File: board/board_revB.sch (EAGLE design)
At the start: 79 parts, among them Q1 ULN2003AS, Q2 ULN2003AD, Y1 8Mhz

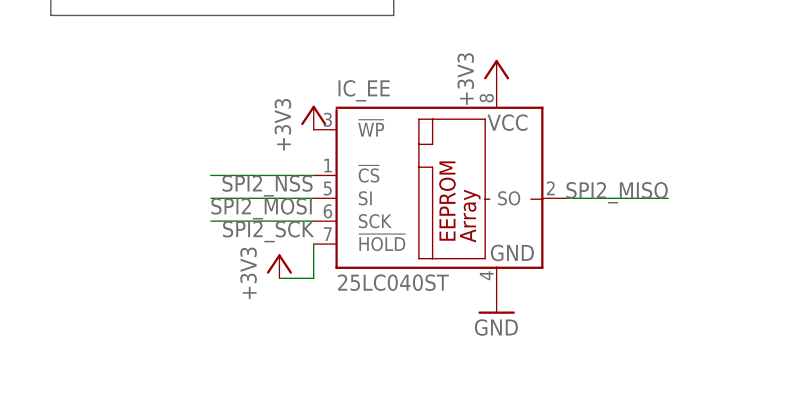
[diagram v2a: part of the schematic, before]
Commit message: [GUI] Working on XML file saving
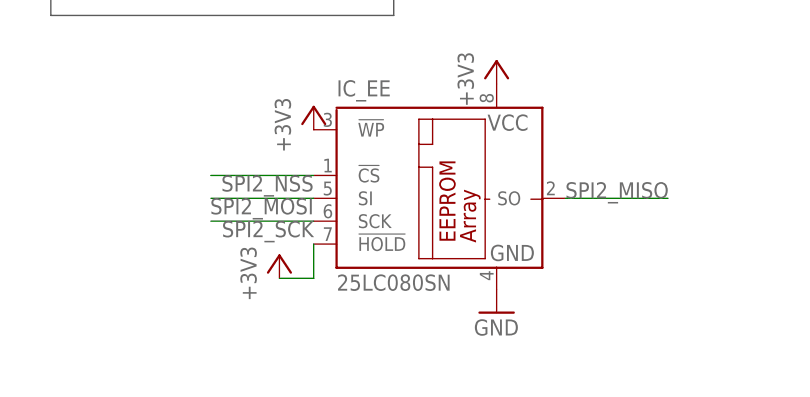
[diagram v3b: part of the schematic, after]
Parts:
- IC_EE: value 25LC040ST -> 25LC080SN; device microchip:25LC040ST -> microchip:25LC080SN
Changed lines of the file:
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@@
 <?xml version="1.0" encoding="utf-8"?>
 <!DOCTYPE eagle SYSTEM "eagle.dtd">
-<eagle version="7.0.0">
+<eagle version="7.1.0">
 <drawing>
 <settings>
@@
 <grid distance="0.05" unitdist="inch" unit="inch" style="lines" multiple="1" display="yes" altdistance="0.005" altunitdist="inch" altunit="inch"/>
 <layers>
-<layer number="1" name="Top" color="4" fill="1" visible="no" active="no"/>
-<layer number="2" name="Route2" color="1" fill="3" visible="no" active="no"/>
-<layer number="3" name="Route3" color="4" fill="3" visible="no" active="no"/>
-<layer number="4" name="Route4" color="1" fill="4" visible="no" active="no"/>
-<layer number="5" name="Route5" color="4" fill="4" visible="no" active="no"/>
-<layer number="6" name="Route6" color="1" fill="8" visible="no" active="no"/>
-<layer number="7" name="Route7" color="4" fill="8" visible="no" active="no"/>
-<layer number="8" name="Route8" color="1" fill="2" visible="no" active="no"/>
-<layer number="9" name="Route9" color="4" fill="2" visible="no" active="no"/>
-<layer number="10" name="Route10" color="1" fill="7" visible="no" active="no"/>
-<layer number="11" name="Route11" color="4" fill="7" visible="no" active="no"/>
-<layer number="12" name="Route12" color="1" fill="5" visible="no" active="no"/>
-<layer number="13" name="Route13" color="4" fill="5" visible="no" active="no"/>
-<layer number="14" name="Route14" color="1" fill="6" visible="no" active="no"/>
-<layer number="15" name="Route15" color="4" fill="6" visible="no" active="no"/>
-<layer number="16" name="Bottom" color="1" fill="1" visible="no" active="no"/>
-<layer number="17" name="Pads" color="2" fill="1" visible="no" active="no"/>
-<layer number="18" name="Vias" color="2" fill="1" visible="no" active="no"/>
-<layer number="19" name="Unrouted" color="6" fill="1" visible="no" active="no"/>
-<layer number="20" name="Dimension" color="15" fill="1" visible="no" active="no"/>
-<layer number="21" name="tPlace" color="16" fill="1" visible="no" active="no"/>
-<layer number="22" name="bPlace" color="14" fill="1" visible="no" active="no"/>
-<layer number="23" name="tOrigins" color="15" fill="1" visible="no" active="no"/>
-<layer number="24" name="bOrigins" color="15" fill="1" visible="no" active="no"/>
-<layer number="25" name="tNames" color="7" fill="1" visible="no" active="no"/>
-<layer number="26" name="bNames" color="7" fill="1" visible="no" active="no"/>
-<layer number="27" name="tValues" color="7" fill="1" visible="no" active="no"/>
-<layer number="28" name="bValues" color="7" fill="1" visible="no" active="no"/>
+<layer number="1" name="Top" color="4" fill="1" visible="yes" active="no"/>
+<layer number="2" name="Route2" color="1" fill="3" visible="yes" active="no"/>
+<layer number="3" name="Route3" color="4" fill="3" visible="yes" active="no"/>
+<layer number="4" name="Route4" color="1" fill="4" visible="yes" active="no"/>
+<layer number="5" name="Route5" color="4" fill="4" visible="yes" active="no"/>
+<layer number="6" name="Route6" color="1" fill="8" visible="yes" active="no"/>
+<layer number="7" name="Route7" color="4" fill="8" visible="yes" active="no"/>
+<layer number="8" name="Route8" color="1" fill="2" visible="yes" active="no"/>
+<layer number="9" name="Route9" color="4" fill="2" visible="yes" active="no"/>
+<layer number="10" name="Route10" color="1" fill="7" visible="yes" active="no"/>
+<layer number="11" name="Route11" color="4" fill="7" visible="yes" active="no"/>
+<layer number="12" name="Route12" color="1" fill="5" visible="yes" active="no"/>
+<layer number="13" name="Route13" color="4" fill="5" visible="yes" active="no"/>
+<layer number="14" name="Route14" color="1" fill="6" visible="yes" active="no"/>
+<layer number="15" name="Route15" color="4" fill="6" visible="yes" active="no"/>
+<layer number="16" name="Bottom" color="1" fill="1" visible="yes" active="no"/>
+<layer number="17" name="Pads" color="2" fill="1" visible="yes" active="no"/>
+<layer number="18" name="Vias" color="2" fill="1" visible="yes" active="no"/>
+<layer number="19" name="Unrouted" color="6" fill="1" visible="yes" active="no"/>
+<layer number="20" name="Dimension" color="15" fill="1" visible="yes" active="no"/>
+<layer number="21" name="tPlace" color="16" fill="1" visible="yes" active="no"/>
+<layer number="22" name="bPlace" color="14" fill="1" visible="yes" active="no"/>
+<layer number="23" name="tOrigins" color="15" fill="1" visible="yes" active="no"/>
+<layer number="24" name="bOrigins" color="15" fill="1" visible="yes" active="no"/>
+<layer number="25" name="tNames" color="7" fill="1" visible="yes" active="no"/>
+<layer number="26" name="bNames" color="7" fill="1" visible="yes" active="no"/>
+<layer number="27" name="tValues" color="7" fill="1" visible="yes" active="no"/>
+<layer number="28" name="bValues" color="7" fill="1" visible="yes" active="no"/>
 <layer number="29" name="tStop" color="7" fill="3" visible="no" active="no"/>
 <layer number="30" name="bStop" color="7" fill="6" visible="no" active="no"/>
@@
 <layer number="35" name="tGlue" color="7" fill="4" visible="no" active="no"/>
 <layer number="36" name="bGlue" color="7" fill="5" visible="no" active="no"/>
-<layer number="37" name="tTest" color="7" fill="1" visible="no" active="no"/>
-<layer number="38" name="bTest" color="7" fill="1" visible="no" active="no"/>
+<layer number="37" name="tTest" color="7" fill="1" visible="yes" active="no"/>
+<layer number="38" name="bTest" color="7" fill="1" visible="yes" active="no"/>
 <layer number="39" name="tKeepout" color="4" fill="11" visible="no" active="no"/>
 <layer number="40" name="bKeepout" color="1" fill="11" visible="no" active="no"/>
@@
 <layer number="44" name="Drills" color="7" fill="1" visible="no" active="no"/>
 <layer number="45" name="Holes" color="7" fill="1" visible="no" active="no"/>
-<layer number="46" name="Milling" color="3" fill="1" visible="no" active="no"/>
-<layer number="47" name="Measures" color="7" fill="1" visible="no" active="no"/>
-<layer number="48" name="Document" color="7" fill="1" visible="no" active="no"/>
-<layer number="49" name="Reference" color="7" fill="1" visible="no" active="no"/>
-<layer number="50" name="dxf" color="7" fill="1" visible="no" active="no"/>
-<layer number="51" name="tDocu" color="6" fill="1" visible="no" active="no"/>
-<layer number="52" name="bDocu" color="7" fill="1" visible="no" active="no"/>
-<layer number="53" name="tGND_GNDA" color="7" fill="9" visible="no" active="no"/>
-<layer number="54" name="bGND_GNDA" color="1" fill="9" visible="no" active="no"/>
-<layer number="56" name="wert" color="7" fill="1" visible="no" active="no"/>
-<layer number="57" name="tCAD" color="7" fill="1" visible="no" active="no"/>
+<layer number="46" name="Milling" color="3" fill="1" visible="yes" active="no"/>
+<layer number="47" name="Measures" color="7" fill="1" visible="yes" active="no"/>
+<layer number="48" name="Document" color="7" fill="1" visible="yes" active="no"/>
+<layer number="49" name="Reference" color="7" fill="1" visible="yes" active="no"/>
+<layer number="50" name="dxf" color="7" fill="1" visible="yes" active="no"/>
+<layer number="51" name="tDocu" color="6" fill="1" visible="yes" active="no"/>
+<layer number="52" name="bDocu" color="7" fill="1" visible="yes" active="no"/>
+<layer number="53" name="tGND_GNDA" color="7" fill="9" visible="yes" active="no"/>
+<layer number="54" name="bGND_GNDA" color="1" fill="9" visible="yes" active="no"/>
+<layer number="56" name="wert" color="7" fill="1" visible="yes" active="no"/>
+<layer number="57" name="tCAD" color="7" fill="1" visible="yes" active="no"/>
 <layer number="91" name="Nets" color="2" fill="1" visible="yes" active="yes"/>
 <layer number="92" name="Busses" color="1" fill="1" visible="yes" active="yes"/>
@@
 <part name="+3V6" library="supply1" deviceset="+3V3" device=""/>
 <part name="GND22" library="supply1" deviceset="GND" device=""/>
-<part name="IC_EE" library="microchip" deviceset="25*" device="ST" technology="LC040"/>
 <part name="+3V16" library="supply1" deviceset="+3V3" device=""/>
 <part name="+3V18" library="supply1" deviceset="+3V3" device=""/>
+<part name="IC_EE" library="microchip" deviceset="25*" device="SN" technology="LC080"/>
 </parts>
 <sheets>
@@
 <instance part="+3V6" gate="G$1" x="264.16" y="38.1"/>
 <instance part="GND22" gate="1" x="264.16" y="10.16"/>
-<instance part="IC_EE" gate="G$1" x="256.54" y="22.86"/>
 <instance part="+3V16" gate="G$1" x="243.84" y="33.02"/>
 <instance part="+3V18" gate="G$1" x="240.03" y="16.51"/>
+<instance part="IC_EE" gate="G$1" x="256.54" y="22.86"/>
 </instances>
 <busses>
@@
 </segment>
 <segment>
+<pinref part="GND22" gate="1" pin="GND"/>
 <pinref part="IC_EE" gate="G$1" pin="GND"/>
-<pinref part="GND22" gate="1" pin="GND"/>
 </segment>
 </net>
@@
 </segment>
 <segment>
+<pinref part="+3V18" gate="G$1" pin="+3V3"/>
+<wire x1="240.03" y1="13.97" x2="243.84" y2="13.97" width="0.1524" layer="91"/>
+<wire x1="243.84" y1="13.97" x2="243.84" y2="17.78" width="0.1524" layer="91"/>
+<pinref part="IC_EE" gate="G$1" pin="!HOLD"/>
+</segment>
+<segment>
 <pinref part="+3V6" gate="G$1" pin="+3V3"/>
 <pinref part="IC_EE" gate="G$1" pin="VCC"/>
 </segment>
 <segment>
+<pinref part="+3V16" gate="G$1" pin="+3V3"/>
 <pinref part="IC_EE" gate="G$1" pin="!WP"/>
-<pinref part="+3V16" gate="G$1" pin="+3V3"/>
-</segment>
-<segment>
-<pinref part="+3V18" gate="G$1" pin="+3V3"/>
-<pinref part="IC_EE" gate="G$1" pin="!HOLD"/>
-<wire x1="240.03" y1="13.97" x2="243.84" y2="13.97" width="0.1524" layer="91"/>
-<wire x1="243.84" y1="13.97" x2="243.84" y2="17.78" width="0.1524" layer="91"/>
 </segment>
 </net>
@@
 <segment>
 <label x="243.84" y="25.4" size="1.778" layer="95" rot="R180"/>
+<wire x1="232.41" y1="25.4" x2="243.84" y2="25.4" width="0.1524" layer="91"/>
 <pinref part="IC_EE" gate="G$1" pin="!CS"/>
-<wire x1="232.41" y1="25.4" x2="243.84" y2="25.4" width="0.1524" layer="91"/>
-</segment>
-</net>
+</segment>
+</net>

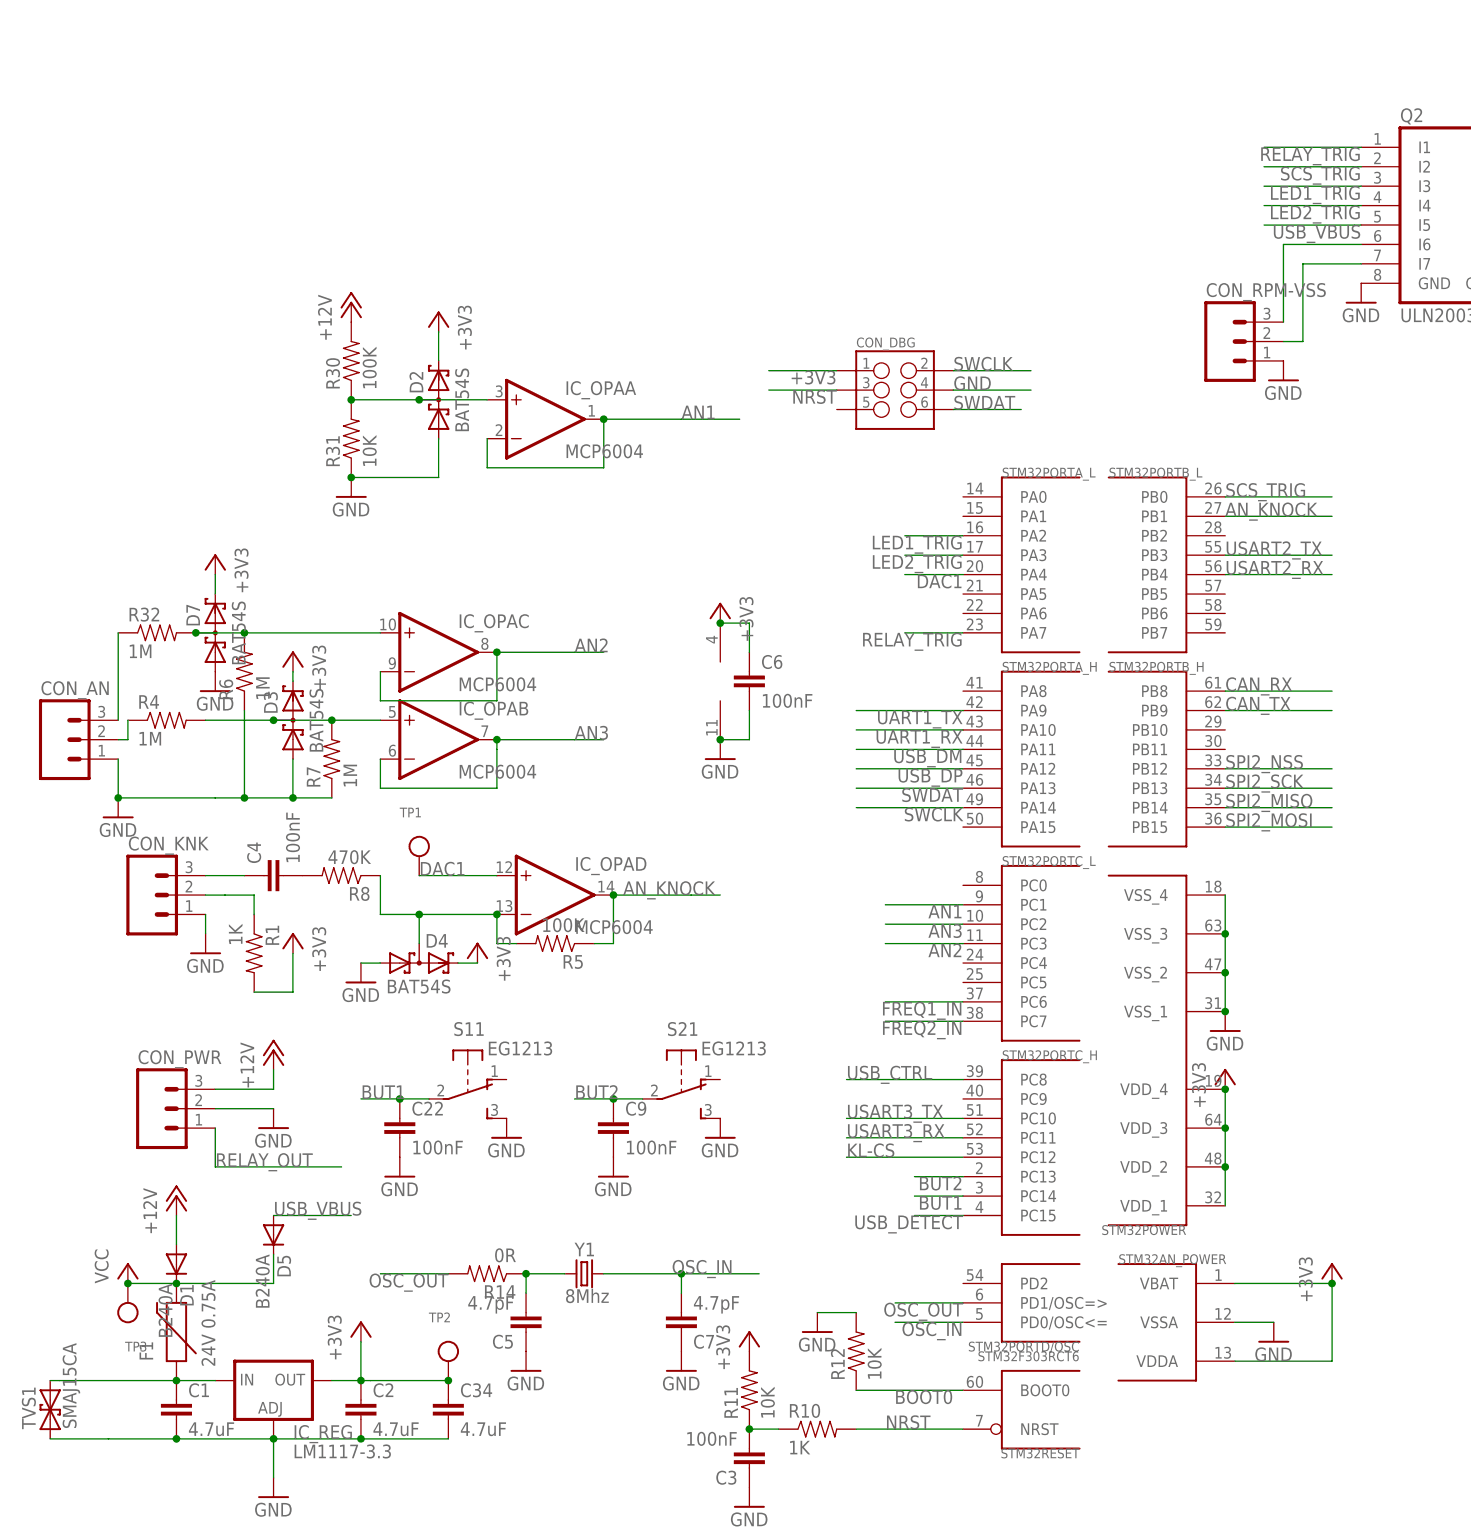
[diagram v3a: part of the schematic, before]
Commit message: [GUI/Code] Rewrote DSP functions, switched to float; Updated DSP library
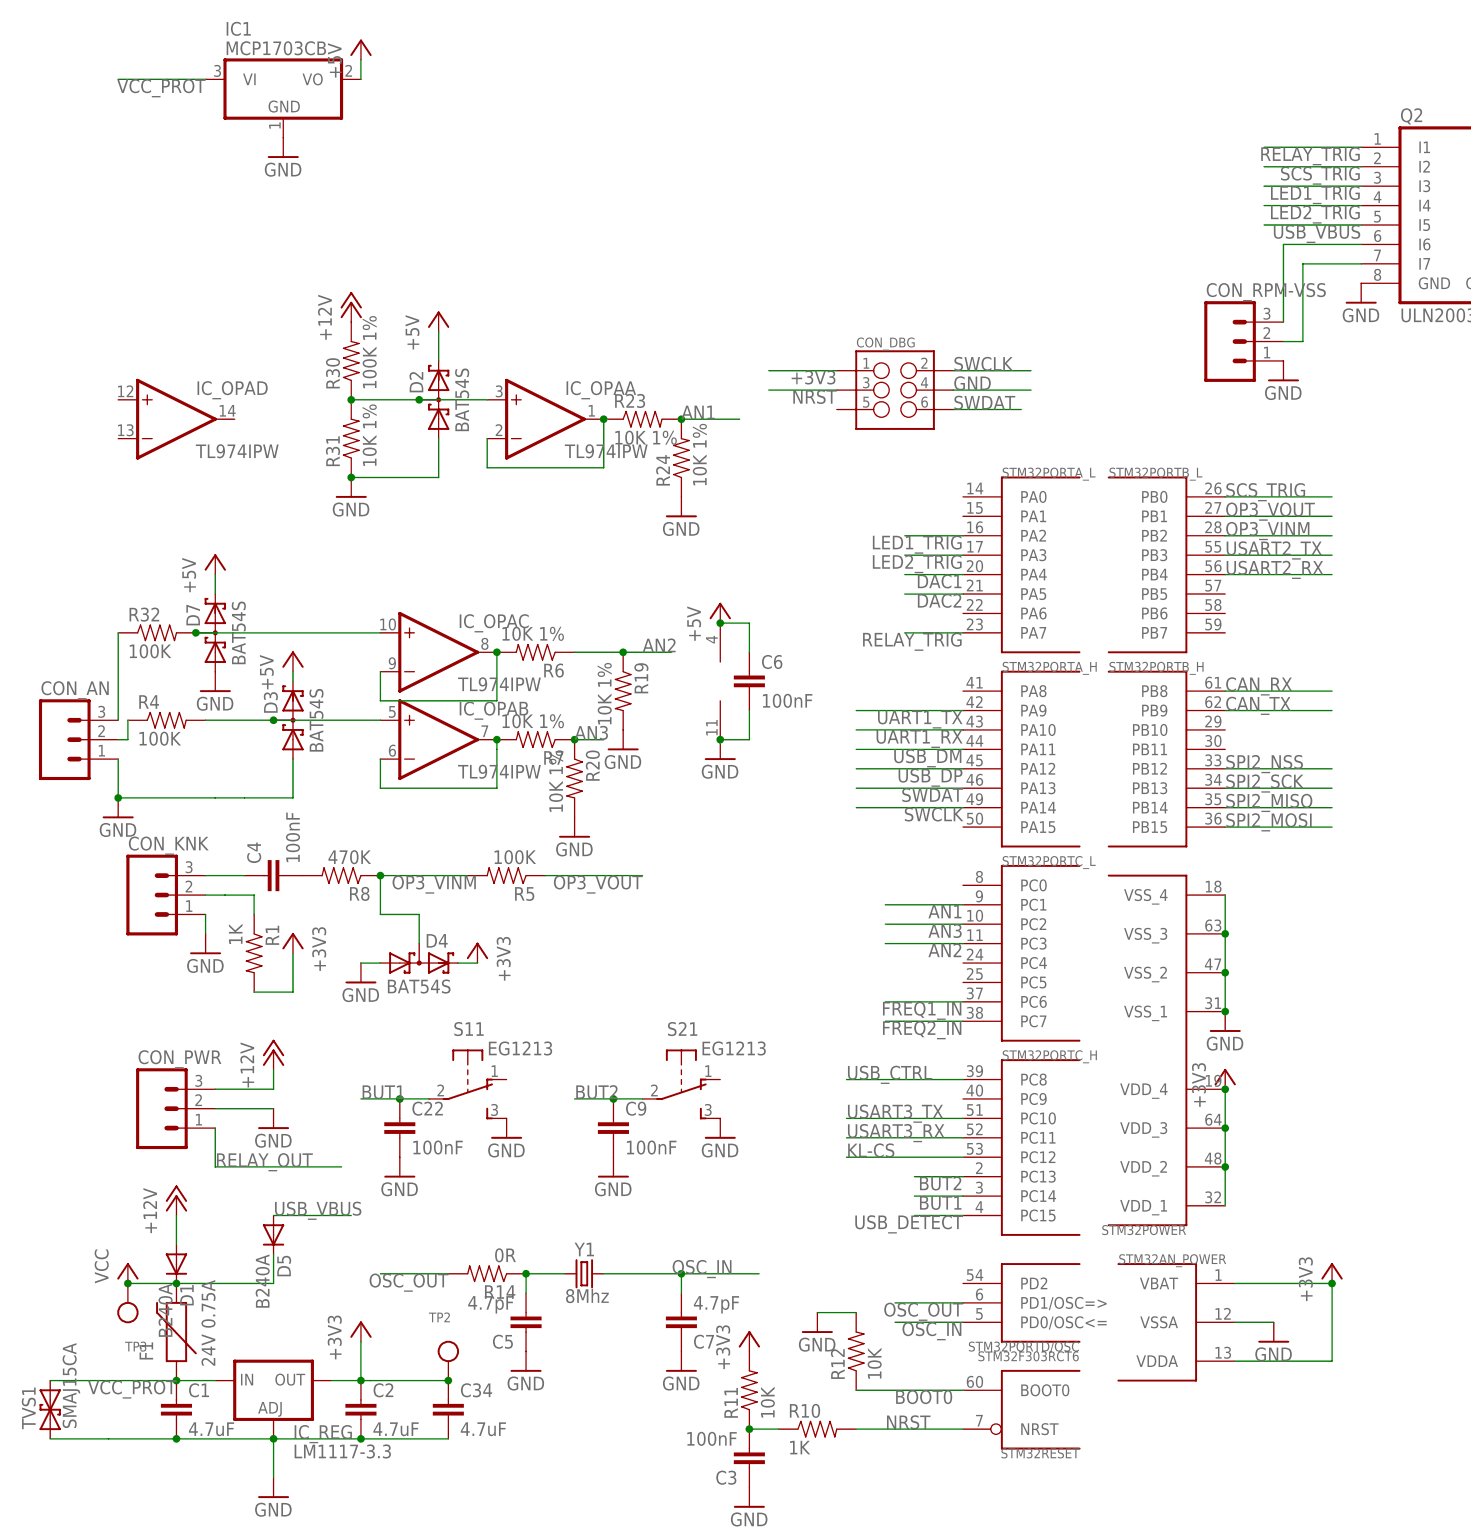
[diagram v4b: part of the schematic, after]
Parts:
- removed TP1: (no value), microbuilder:TESTPOINTROUND1MM
- added IC1: MCP1703CB, linear:MCP1703CB
- added R19, R20, R23, R24: 10K 1%, SparkFun-Resistors:RESISTOR0603-RES
- IC_OPA: value MCP6004 -> TL974IPW
- R30: value 100K -> 100K 1%
- R31: value 10K -> 10K 1%
- R32, R4: value 1M -> 100K
- R6, R7: value 1M -> 10K 1%
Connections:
- removed net AN_KNOCK: IC_OPAD.OUT, R5.1, STM32PORTB_L.PB1
- removed net N$12: D4.C1A2, IC_OPAD.-IN, R5.2, R8.1
- removed net N$20: C1.1, F1.1, IC_REG.IN, TVS1.2
- new net +5V: C6.1, D2.C2, D3.C2, D7.C2, IC1.VO, IC_OPAP.V+
- new net AN1_N: IC_OPAA.-IN, IC_OPAA.OUT, R23.1
- new net AN2_N: IC_OPAC.-IN, IC_OPAC.OUT, R6.2
- new net AN3_N: IC_OPAB.-IN, IC_OPAB.OUT, R7.2
- new net DAC2: STM32PORTA_L.PA5
- new net OP3_VINM: D4.C1A2, R5.2, R8.1, STM32PORTB_L.PB2
- new net OP3_VOUT: R5.1, STM32PORTB_L.PB1
- new net VCC_PROT: C1.1, F1.1, IC1.VI, IC_REG.IN, TVS1.2
- net +3V3: no longer C6.1, D2.C2, D3.C2, D7.C2, IC_OPAP.V+
- net AN1: now also R23.2, R24.2; no longer IC_OPAA.-IN, IC_OPAA.OUT
- net AN2: now also R19.1, R6.1; no longer IC_OPAC.-IN, IC_OPAC.OUT
- net AN3: now also R20.1, R7.1; no longer IC_OPAB.-IN, IC_OPAB.OUT
- net DAC1: no longer IC_OPAD.+IN, TP1.P$1
- net GND: now also IC1.GND, R19.2, R20.2, R24.1; no longer R6.1, R7.1
- net N$25: no longer R6.2
- net N$5: no longer R7.2
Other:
- moved on the sheet: IC_OPAD, R5, R6, R7
